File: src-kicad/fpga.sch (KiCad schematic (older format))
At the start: 11 parts, among them U1 iCE40HX1K-TQ144

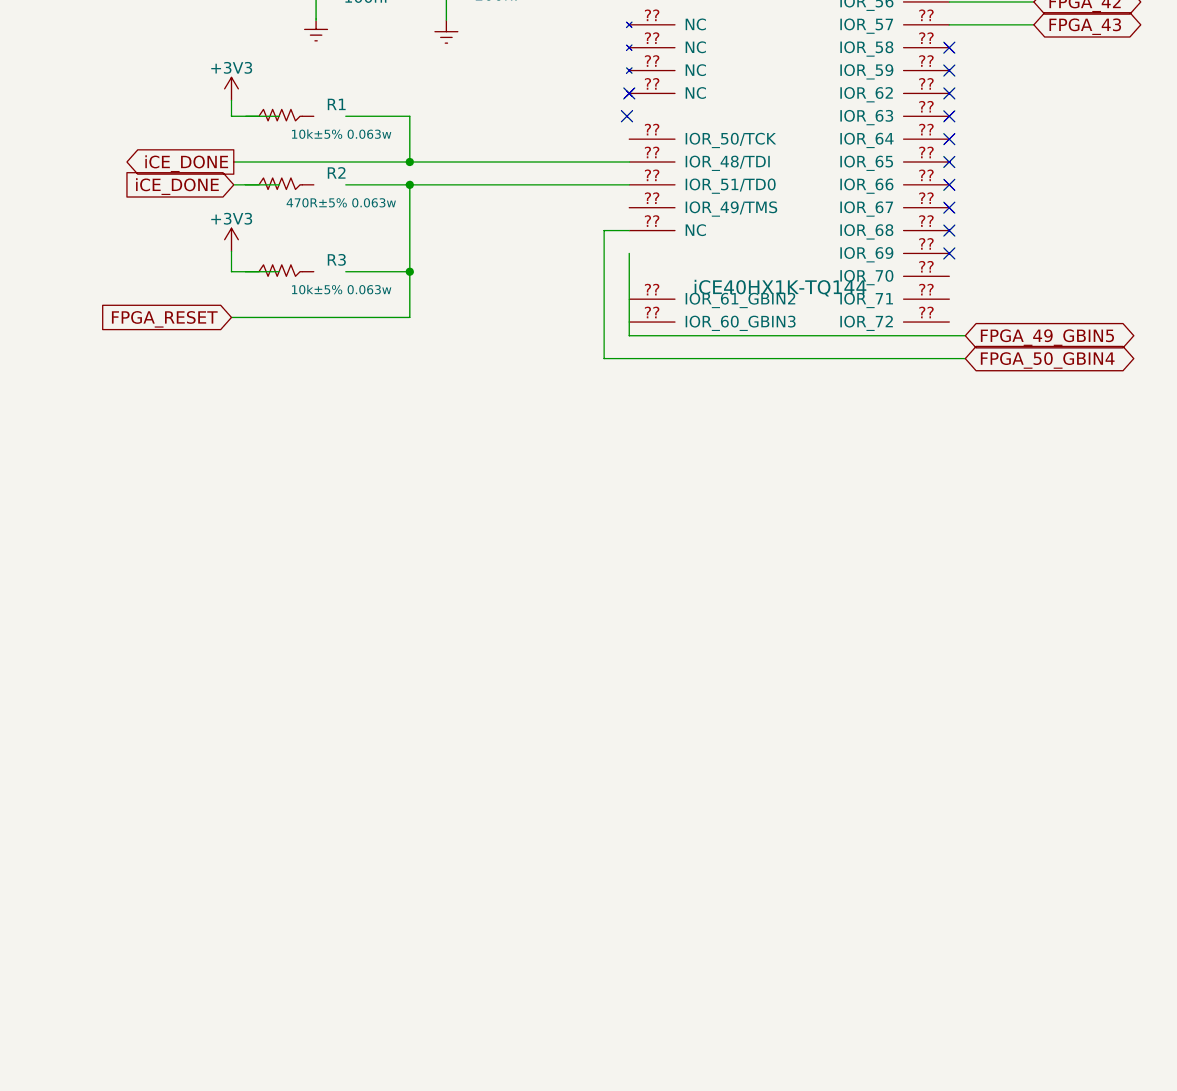
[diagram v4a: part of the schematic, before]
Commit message: Kicad. FPGA bank3 added
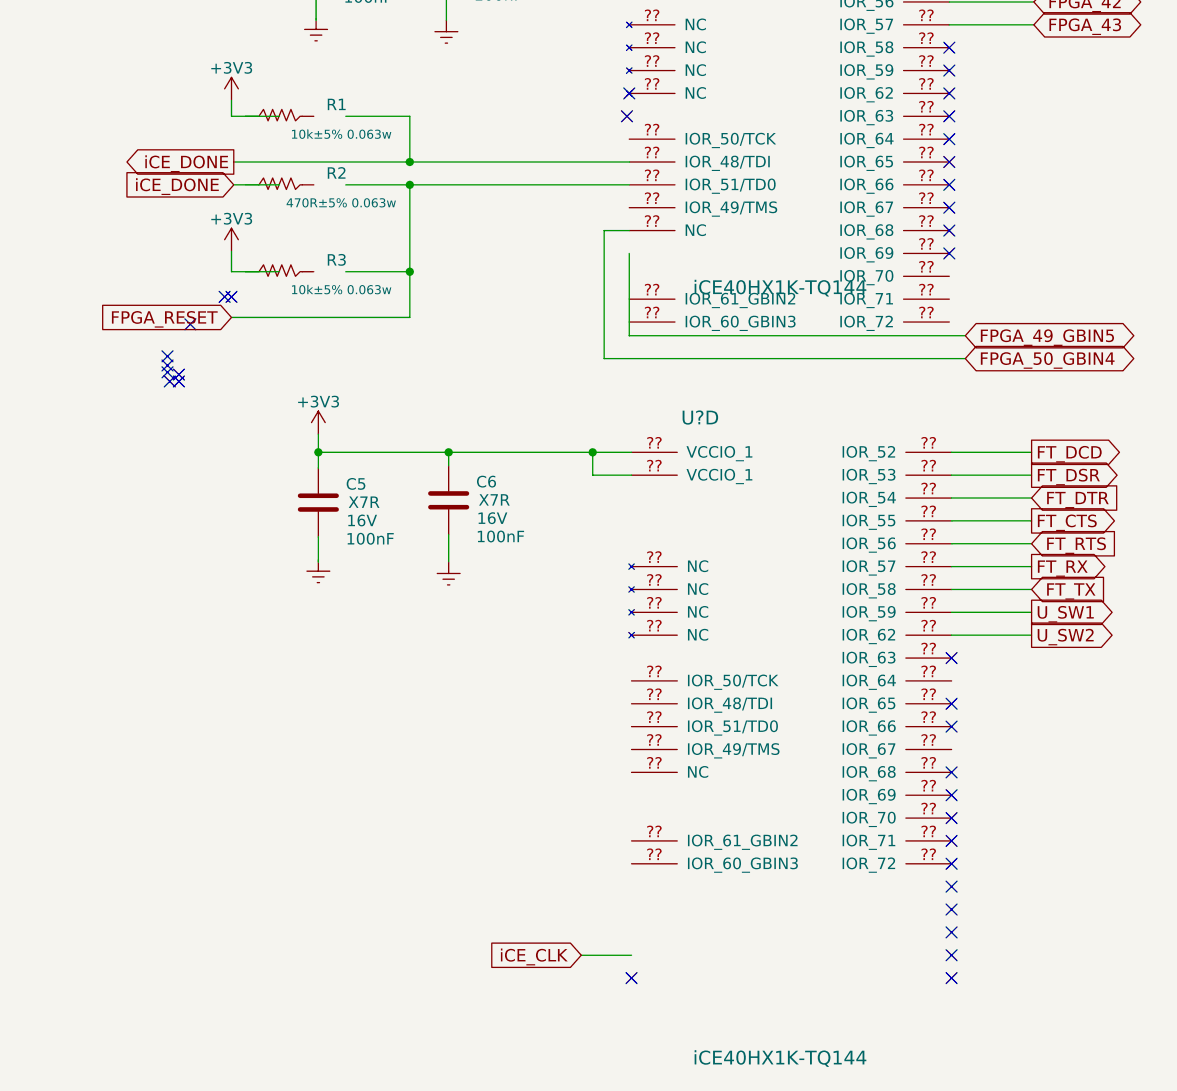
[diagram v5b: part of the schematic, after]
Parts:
- added C5, C6: 100nF, symbol C
- added U?: iCE40HX1K-TQ144, symbol iCE40HX1K-TQ144
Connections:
- net labels added: FT_CTS, FT_DCD, FT_DSR, FT_DTR, FT_RTS, FT_RX, FT_TX, U_SW1, U_SW2, iCE_CLK
- wire segments 78 -> 95
- no-connect marks 29 -> 52
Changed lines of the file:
@@
 	7490 1090 7250 1090
 Wire Wire Line
-	7490 2090 5760 2090
+	5760 2090 7490 2090
 Wire Wire Line
 	5750 1820 5750 1890
@@
 Wire Wire Line
 	7380 2950 8960 2950
+$Comp
+L iCE40HX1K-TQ144 U?
+U 4 1 5743EEA2
+P 7500 3360
+F 0 "U?" H 7800 3510 60  0000 C CNN
+F 1 "iCE40HX1K-TQ144" H 8150 710 60  0000 C CNN
+F 2 "" H 7800 2060 60  0000 C CNN
+F 3 "" H 7800 2060 60  0000 C CNN
+	4    7500 3360
+	1    0    0    -1
+$EndComp
+$Comp
+L C C5
+U 1 1 5743FA51
+P 6130 3580
+F 0 "C5" H 6250 3660 50  0000 L CNN
+F 1 "100nF" H 6250 3420 50  0000 L CNN
+F 2 "" H 6168 3430 50  0000 C CNN
+F 3 "" H 6130 3580 50  0000 C CNN
+F 4 "X7R" H 6330 3580 50  0000 C CNN "class"
+F 5 "16V" H 6320 3500 50  0000 C CNN "Voltage"
+	1    6130 3580
+	1    0    0    -1
+$EndComp
+$Comp
+L +3V3 #PWR?
+U 1 1 5743FA57
+P 6130 3280
+F 0 "#PWR?" H 6130 3130 50  0001 C CNN
+F 1 "+3V3" H 6130 3420 50  0000 C CNN
+F 2 "" H 6130 3280 50  0000 C CNN
+F 3 "" H 6130 3280 50  0000 C CNN
+	1    6130 3280
+	1    0    0    -1
+$EndComp
+$Comp
+L GNDREF #PWR?
+U 1 1 5743FA5D
+P 6130 3830
+F 0 "#PWR?" H 6130 3580 50  0001 C CNN
+F 1 "GNDREF" H 6130 3680 50  0001 C CNN
+F 2 "" H 6130 3830 50  0000 C CNN
+F 3 "" H 6130 3830 50  0000 C CNN
+	1    6130 3830
+	1    0    0    -1
+$EndComp
+$Comp
+L C C6
+U 1 1 5743FA65
+P 6700 3570
+F 0 "C6" H 6820 3650 50  0000 L CNN
+F 1 "100nF" H 6820 3410 50  0000 L CNN
+F 2 "" H 6738 3420 50  0000 C CNN
+F 3 "" H 6700 3570 50  0000 C CNN
+F 4 "X7R" H 6900 3570 50  0000 C CNN "class"
+F 5 "16V" H 6890 3490 50  0000 C CNN "Voltage"
+	1    6700 3570
+	1    0    0    -1
+$EndComp
+$Comp
+L GNDREF #PWR?
+U 1 1 5743FA6B
+P 6700 3840
+F 0 "#PWR?" H 6700 3590 50  0001 C CNN
+F 1 "GNDREF" H 6700 3690 50  0001 C CNN
+F 2 "" H 6700 3840 50  0000 C CNN
+F 3 "" H 6700 3840 50  0000 C CNN
+	1    6700 3840
+	1    0    0    -1
+$EndComp
+Wire Wire Line
+	6130 3280 6130 3430
+Wire Wire Line
+	6130 3840 6130 3730
+Wire Wire Line
+	6700 3720 6700 3840
+Wire Wire Line
+	6130 3360 7500 3360
+Connection ~ 6130 3360
+Wire Wire Line
+	6700 3420 6700 3360
+Connection ~ 6700 3360
+Wire Wire Line
+	7500 3460 7330 3460
+Wire Wire Line
+	7330 3460 7330 3360
+Connection ~ 7330 3360
+Text GLabel 9250 3360 2    54   Output ~ 0
+FT_DCD
+Wire Wire Line
+	8900 3360 9250 3360
+Text GLabel 9250 3460 2    54   Output ~ 0
+FT_DSR
+Wire Wire Line
+	8900 3460 9250 3460
+Text GLabel 9250 3560 2    54   Input ~ 0
+FT_DTR
+Wire Wire Line
+	8900 3560 9250 3560
+Text GLabel 9250 3660 2    54   Output ~ 0
+FT_CTS
+Wire Wire Line
+	8900 3660 9250 3660
+Text GLabel 9250 3760 2    54   Input ~ 0
+FT_RTS
+Wire Wire Line
+	8900 3760 9250 3760
+Text GLabel 9250 3860 2    54   Output ~ 0
+FT_RX
+Wire Wire Line
+	9250 3860 8900 3860
+Text GLabel 9250 3960 2    54   Input ~ 0
+FT_TX
+Wire Wire Line
+	8900 3960 9250 3960
+Text GLabel 9250 4060 2    54   Output ~ 0
+U_SW1
+Text GLabel 9250 4160 2    54   Output ~ 0
+U_SW2
+Wire Wire Line
+	9250 4060 8900 4060
+Wire Wire Line
+	9250 4160 8900 4160
+NoConn ~ 8900 4260
+NoConn ~ 5750 2680
+NoConn ~ 5720 2680
+NoConn ~ 5570 2800
+NoConn ~ 5470 2940
+NoConn ~ 5470 2980
+NoConn ~ 5470 3010
+NoConn ~ 5480 3050
+NoConn ~ 5520 3050
+NoConn ~ 5520 3020
+NoConn ~ 8900 4460
+NoConn ~ 8900 4560
+NoConn ~ 8900 4760
+NoConn ~ 8900 4860
+NoConn ~ 8900 4960
+NoConn ~ 8900 5060
+NoConn ~ 8900 5160
+NoConn ~ 8900 5260
+NoConn ~ 8900 5360
+NoConn ~ 8900 5460
+NoConn ~ 8900 5560
+NoConn ~ 8900 5660
+NoConn ~ 7500 5660
+Text GLabel 7280 5560 0    54   Input ~ 0
+iCE_CLK
+Wire Wire Line
+	7280 5560 7500 5560
 $EndSCHEMATC

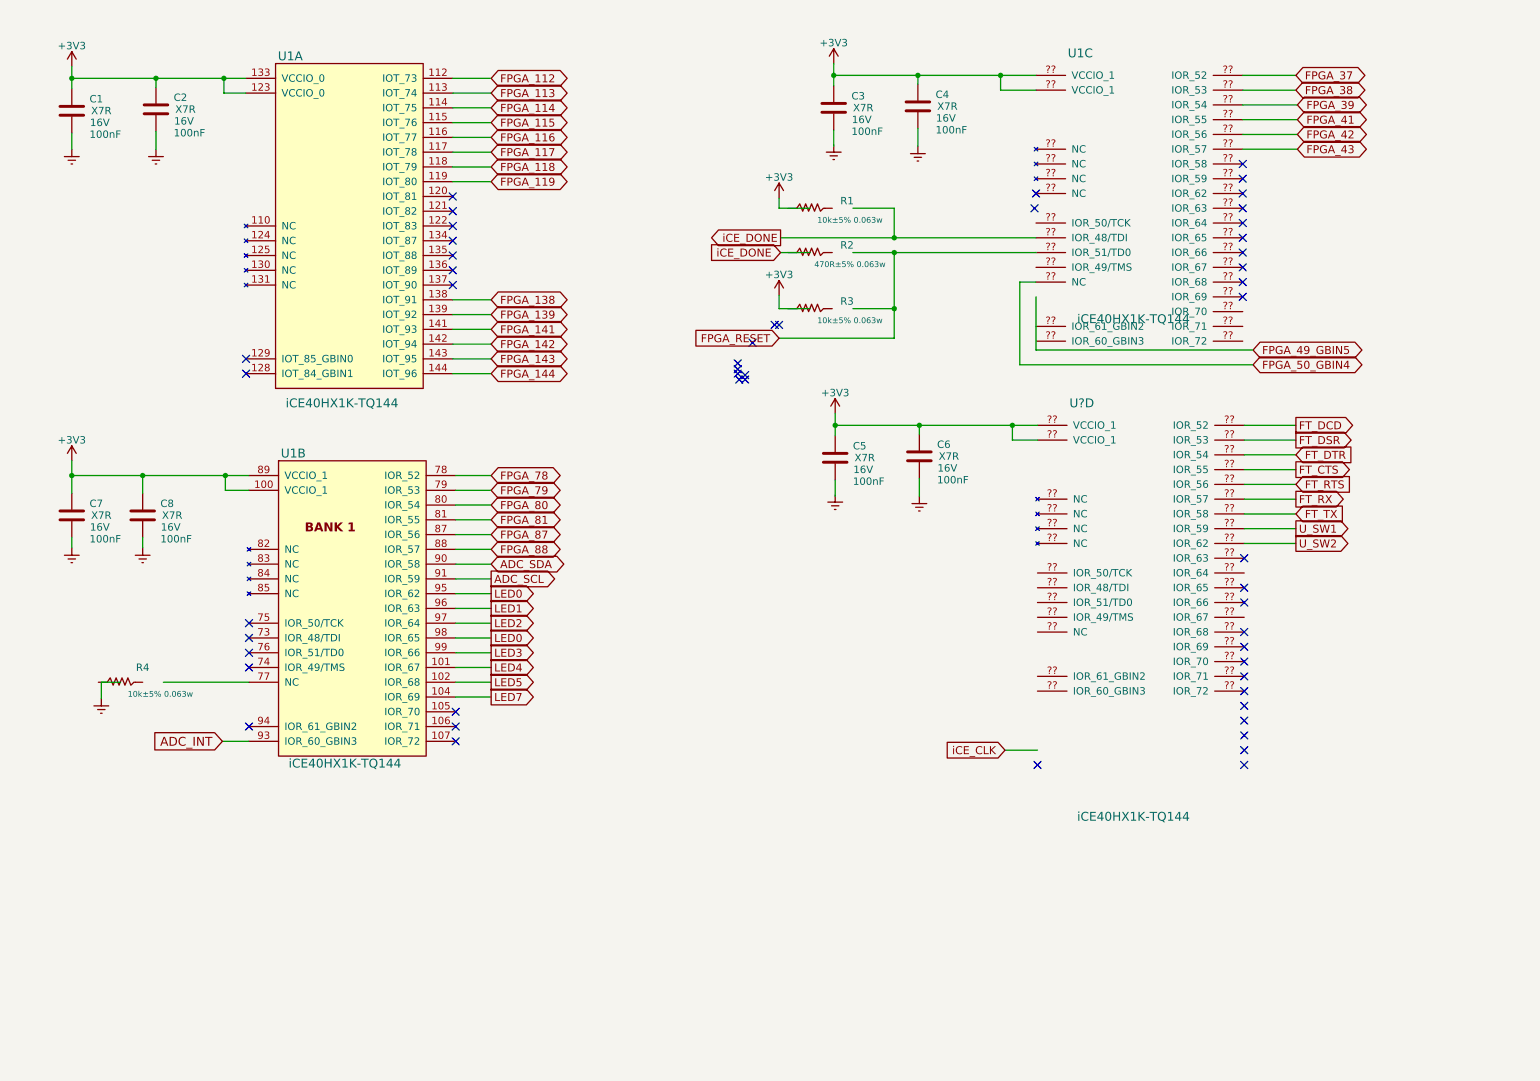
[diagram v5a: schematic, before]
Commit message: Kicad migration. FPGA power module
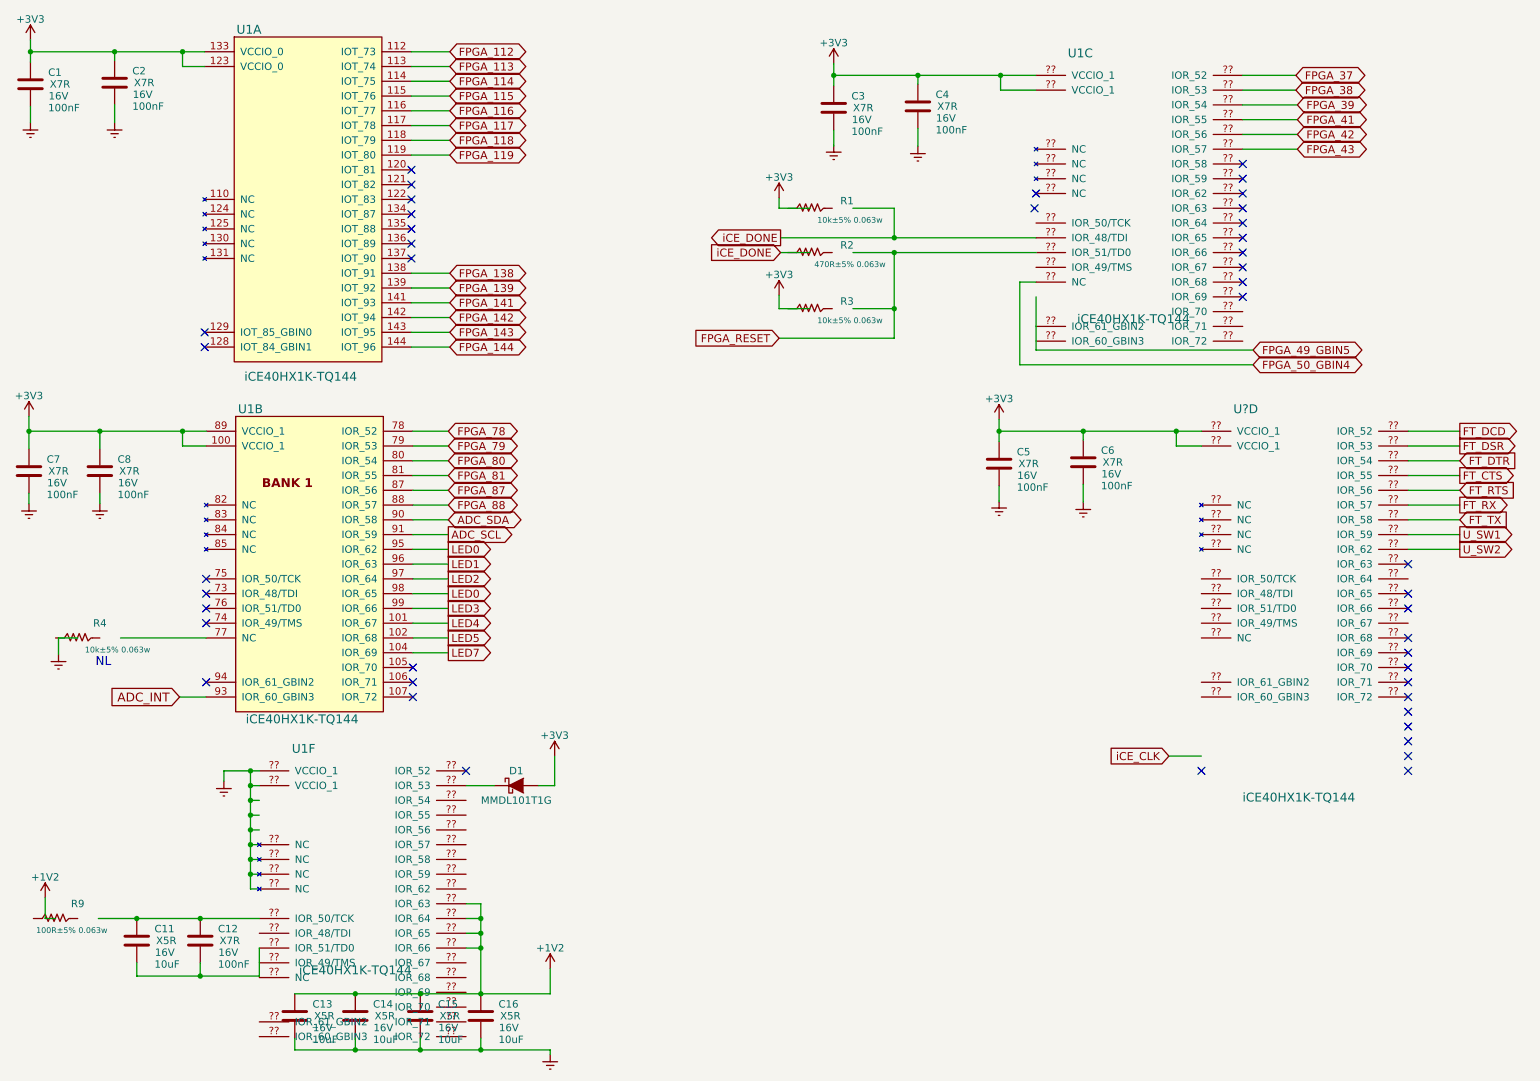
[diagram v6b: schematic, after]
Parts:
- added C11, C13, C14, C15, C16: 10uF, symbol C
- added C12: 100nF, symbol C
- added D1: MMDL101T1G, symbol D_Schottky
- added R9: 100R±5% 0.063w, symbol R
- added unit 6 of U1
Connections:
- net labels added: +1V2
- wire segments 95 -> 129
- no-connect marks 52 -> 44
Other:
- note added: "NL"
- moved on the sheet: C1, C2, C5, C6, C7, C8, R4, U1A, U1B, U?D
